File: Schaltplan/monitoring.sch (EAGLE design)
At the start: 10 parts, among them IC1 TINY26P, IC2 7805TV

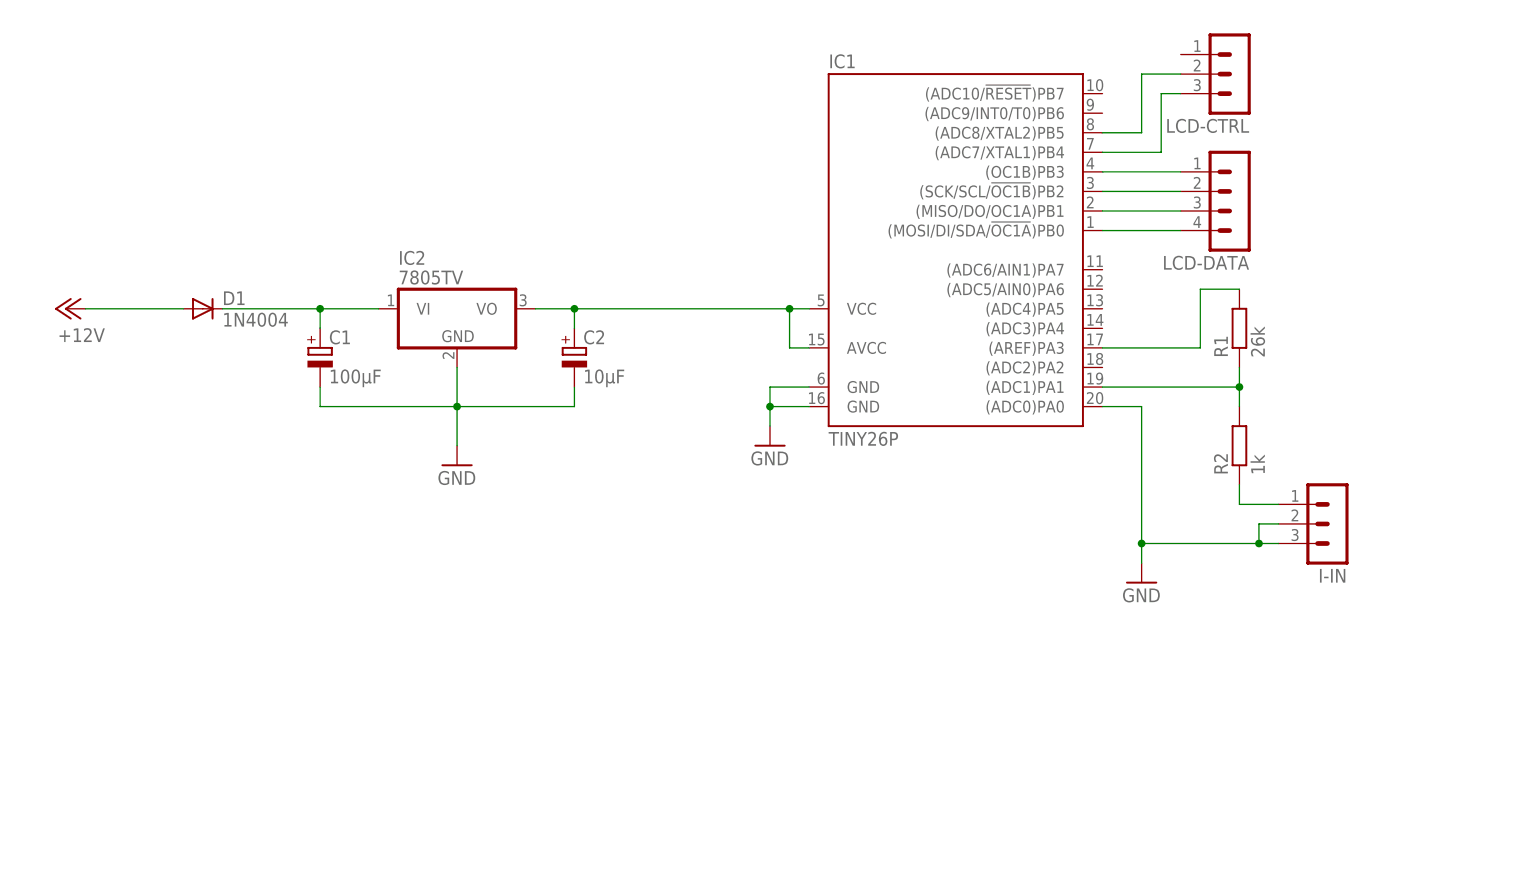
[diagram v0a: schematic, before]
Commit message: Add some induktivits to filter the adc inputs
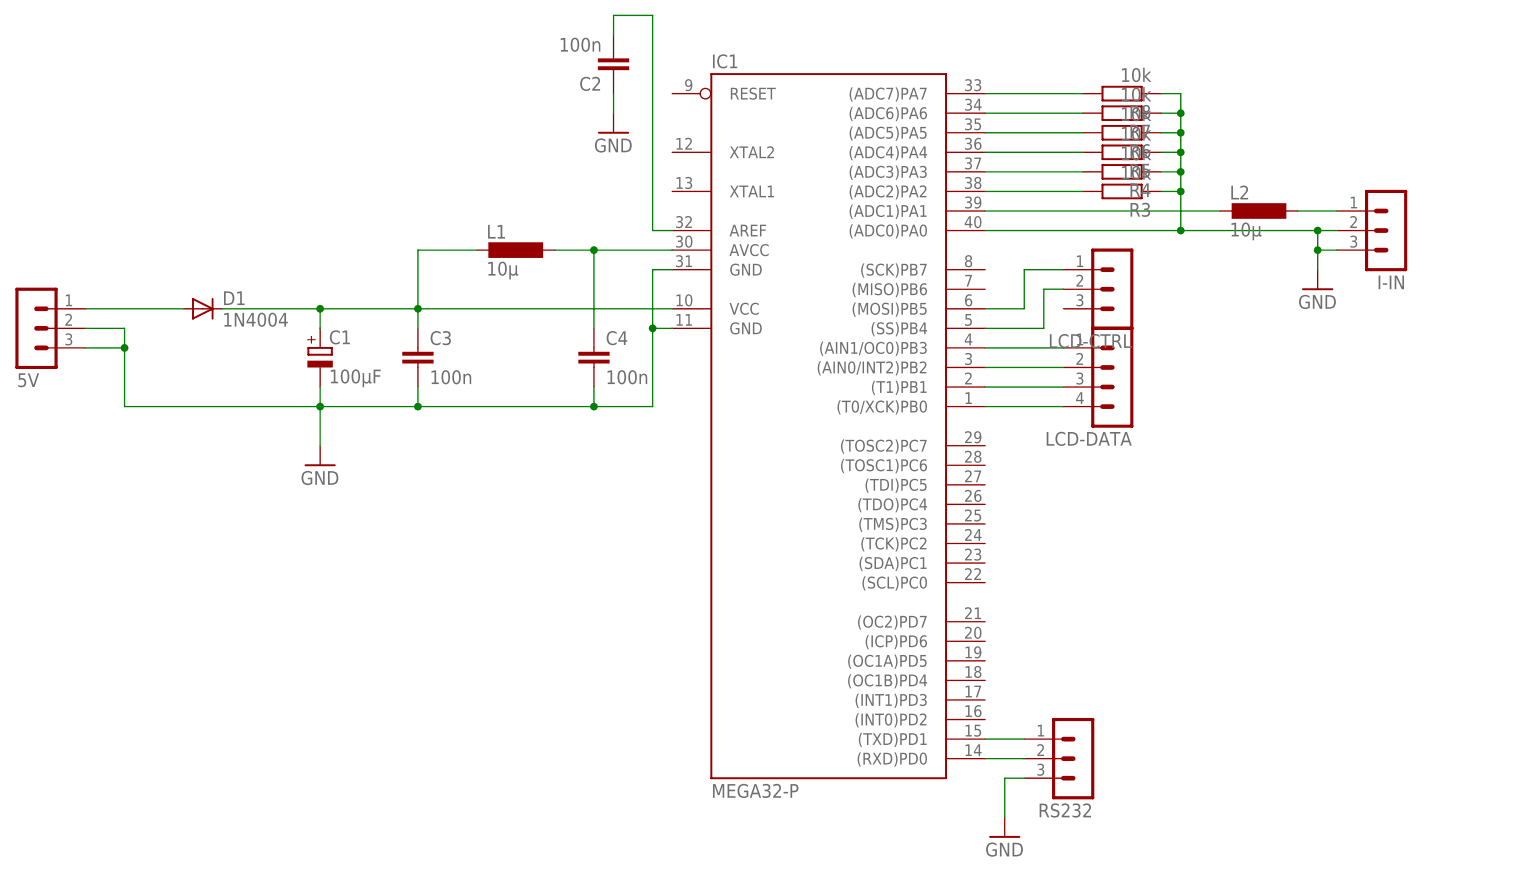
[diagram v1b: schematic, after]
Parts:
- removed IC2: 7805TV, linear:7805TV
- removed R1: 26k, rcl:R-EU_0204/2V
- removed R2: 1k, rcl:R-EU_0204/2V
- added 5V, RS232: (no value), con-lstb:MA03-1
- added C3, C4: 100n, rcl:C-EU050-035X075
- added L1, L2: 10µ, rcl:L-EU0204V
- added R3, R4, R5, R6, R7, R8: 10k, rcl:R-EU_0204/2V
- C2: value 10µF -> 100n; device rcl:CPOL-EUE2.5-7 -> rcl:C-EU050-035X075
- IC1: value TINY26P -> MEGA32-P; device atmel:TINY26P -> atmel:MEGA32-P
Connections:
- removed net +12V: D1.A
- new net N$12: 5V.1, D1.A
- new net N$13: IC1.(ADC4)PA4, R5.2
- new net N$14: C2.2, IC1.AREF
- new net N$15: IC1.(RXD)PD0, RS232.2
- new net N$16: IC1.(TXD)PD1, RS232.1
- new net N$17: IC1.(ADC5)PA5, R6.2
- new net N$18: IC1.(ADC6)PA6, R7.2
- new net N$19: IC1.(ADC7)PA7, R8.2
- new net N$20: C4.1, IC1.AVCC, L1.1
- net GND: now also 5V.2, 5V.3, C2.1, C3.2, C4.2, R3.1, R4.1, R5.1, R6.1, R7.1, R8.1, RS232.3; no longer C2.-, IC2.GND
- net N$1: now also IC1.(AIN1/OC0)PB3, LCD-DATA.1; no longer IC1.(MOSI/DI/SDA/!OC1A!)PB0, LCD-DATA.4
- net N$10: now also IC1.(SS)PB4, LCD-CTRL.2; no longer IC1.(ADC7/XTAL1)PB4, LCD-CTRL.3
- net N$11: now also IC1.(MOSI)PB5, LCD-CTRL.1; no longer IC1.(ADC8/XTAL2)PB5, LCD-CTRL.2
- net N$2: now also C1.+, C3.1, D1.C, L1.2; no longer C2.+, IC1.AVCC, IC2.VO
- net N$3: now also IC1.(ADC2)PA2, R3.2; no longer C1.+, D1.C, IC2.VI
- net N$4: now also IC1.(AIN0/INT2)PB2, LCD-DATA.2; no longer IC1.(MISO/DO/OC1A)PB1, LCD-DATA.3
- net N$5: now also L2.2; no longer R1.1, R2.2
- net N$6: now also IC1.(ADC3)PA3, R4.2; no longer IC1.(AREF)PA3, R1.2
- net N$7: now also L2.1; no longer R2.1
- net N$8: now also IC1.(T1)PB1, LCD-DATA.3; no longer IC1.(SCK/SCL/!OC1B!)PB2, LCD-DATA.2
- net N$9: now also IC1.(T0/XCK)PB0, LCD-DATA.4; no longer IC1.(OC1B)PB3, LCD-DATA.1
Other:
- moved on the sheet: I-IN, LCD-CTRL, LCD-DATA

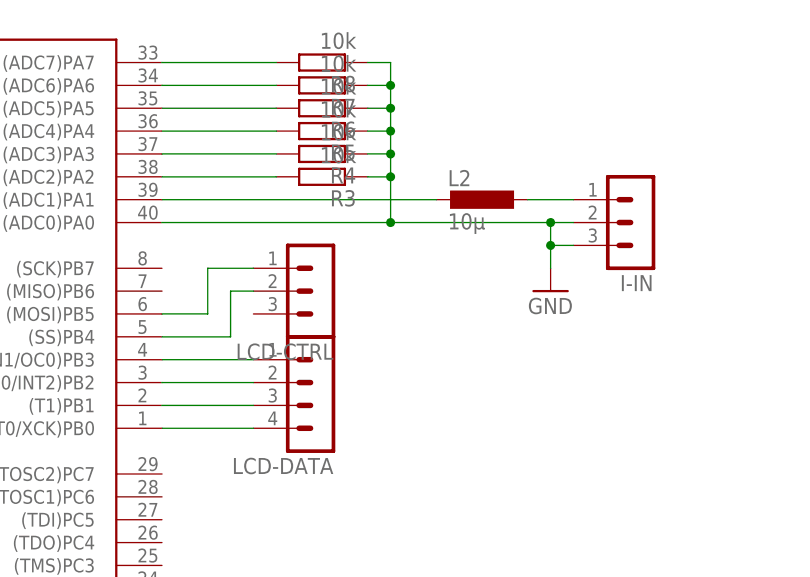
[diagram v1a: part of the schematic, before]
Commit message: Use a median filter and an irr filter for the adc value which measures the current
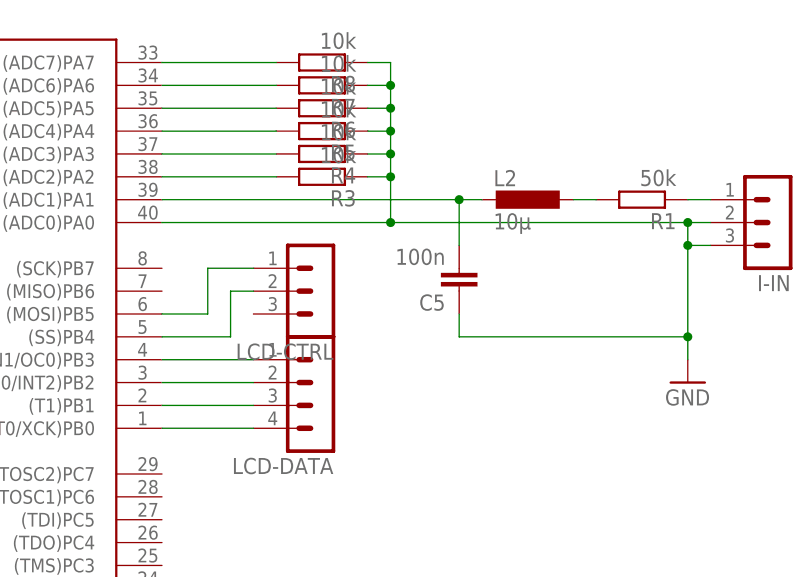
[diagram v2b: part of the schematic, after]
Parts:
- added C5: 100n, rcl:C-EU050-035X075
- added R1: 50k, rcl:R-EU_0204/2V
- L2: device rcl:L-EU0204V -> rcl:L-EU0207/10
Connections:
- removed net N$7: I-IN.1, L2.1
- new net N$21: L2.1, R1.2
- new net N$22: I-IN.1, R1.1
- net GND: now also C5.1
- net N$5: now also C5.2
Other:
- moved on the sheet: I-IN, L2
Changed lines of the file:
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@@
 <grid distance="0.1" unitdist="inch" unit="inch" style="lines" multiple="1" display="no" altdistance="0.01" altunitdist="inch" altunit="inch"/>
 <layers>
-<layer number="1" name="Top" color="4" fill="1" visible="no" active="no"/>
-<layer number="16" name="Bottom" color="1" fill="1" visible="no" active="no"/>
-<layer number="17" name="Pads" color="2" fill="1" visible="no" active="no"/>
-<layer number="18" name="Vias" color="2" fill="1" visible="no" active="no"/>
-<layer number="19" name="Unrouted" color="6" fill="1" visible="no" active="no"/>
-<layer number="20" name="Dimension" color="15" fill="1" visible="no" active="no"/>
-<layer number="21" name="tPlace" color="7" fill="1" visible="no" active="no"/>
-<layer number="22" name="bPlace" color="7" fill="1" visible="no" active="no"/>
-<layer number="23" name="tOrigins" color="15" fill="1" visible="no" active="no"/>
-<layer number="24" name="bOrigins" color="15" fill="1" visible="no" active="no"/>
-<layer number="25" name="tNames" color="7" fill="1" visible="no" active="no"/>
-<layer number="26" name="bNames" color="7" fill="1" visible="no" active="no"/>
-<layer number="27" name="tValues" color="7" fill="1" visible="no" active="no"/>
-<layer number="28" name="bValues" color="7" fill="1" visible="no" active="no"/>
+<layer number="1" name="Top" color="4" fill="1" visible="yes" active="no"/>
+<layer number="16" name="Bottom" color="1" fill="1" visible="yes" active="no"/>
+<layer number="17" name="Pads" color="2" fill="1" visible="yes" active="no"/>
+<layer number="18" name="Vias" color="2" fill="1" visible="yes" active="no"/>
+<layer number="19" name="Unrouted" color="6" fill="1" visible="yes" active="no"/>
+<layer number="20" name="Dimension" color="15" fill="1" visible="yes" active="no"/>
+<layer number="21" name="tPlace" color="7" fill="1" visible="yes" active="no"/>
+<layer number="22" name="bPlace" color="7" fill="1" visible="yes" active="no"/>
+<layer number="23" name="tOrigins" color="15" fill="1" visible="yes" active="no"/>
+<layer number="24" name="bOrigins" color="15" fill="1" visible="yes" active="no"/>
+<layer number="25" name="tNames" color="7" fill="1" visible="yes" active="no"/>
+<layer number="26" name="bNames" color="7" fill="1" visible="yes" active="no"/>
+<layer number="27" name="tValues" color="7" fill="1" visible="yes" active="no"/>
+<layer number="28" name="bValues" color="7" fill="1" visible="yes" active="no"/>
 <layer number="29" name="tStop" color="7" fill="3" visible="no" active="no"/>
 <layer number="30" name="bStop" color="7" fill="6" visible="no" active="no"/>
@@
 <layer number="35" name="tGlue" color="7" fill="4" visible="no" active="no"/>
 <layer number="36" name="bGlue" color="7" fill="5" visible="no" active="no"/>
-<layer number="37" name="tTest" color="7" fill="1" visible="no" active="no"/>
-<layer number="38" name="bTest" color="7" fill="1" visible="no" active="no"/>
+<layer number="37" name="tTest" color="7" fill="1" visible="yes" active="no"/>
+<layer number="38" name="bTest" color="7" fill="1" visible="yes" active="no"/>
 <layer number="39" name="tKeepout" color="4" fill="11" visible="no" active="no"/>
 <layer number="40" name="bKeepout" color="1" fill="11" visible="no" active="no"/>
@@
 <layer number="44" name="Drills" color="7" fill="1" visible="no" active="no"/>
 <layer number="45" name="Holes" color="7" fill="1" visible="no" active="no"/>
-<layer number="46" name="Milling" color="3" fill="1" visible="no" active="no"/>
-<layer number="47" name="Measures" color="7" fill="1" visible="no" active="no"/>
-<layer number="48" name="Document" color="7" fill="1" visible="no" active="no"/>
-<layer number="49" name="Reference" color="7" fill="1" visible="no" active="no"/>
-<layer number="51" name="tDocu" color="7" fill="1" visible="no" active="no"/>
-<layer number="52" name="bDocu" color="7" fill="1" visible="no" active="no"/>
+<layer number="46" name="Milling" color="3" fill="1" visible="yes" active="no"/>
+<layer number="47" name="Measures" color="7" fill="1" visible="yes" active="no"/>
+<layer number="48" name="Document" color="7" fill="1" visible="yes" active="no"/>
+<layer number="49" name="Reference" color="7" fill="1" visible="yes" active="no"/>
+<layer number="51" name="tDocu" color="7" fill="1" visible="yes" active="no"/>
+<layer number="52" name="bDocu" color="7" fill="1" visible="yes" active="no"/>
 <layer number="91" name="Nets" color="2" fill="1" visible="yes" active="yes"/>
 <layer number="92" name="Busses" color="1" fill="1" visible="yes" active="yes"/>
@@
 <part name="C4" library="rcl" deviceset="C-EU" device="050-035X075" value="100n"/>
 <part name="L1" library="rcl" deviceset="L-EU" device="0204V" value="10µ"/>
-<part name="L2" library="rcl" deviceset="L-EU" device="0204V" value="10µ"/>
+<part name="L2" library="rcl" deviceset="L-EU" device="0207/10" value="10µ"/>
+<part name="R1" library="rcl" deviceset="R-EU_" device="0204/2V" value="50k"/>
+<part name="C5" library="rcl" deviceset="C-EU" device="050-035X075" value="100n"/>
 </parts>
 <sheets>
@@
 <instance part="GND1" gate="1" x="-17.78" y="25.4"/>
 <instance part="C1" gate="G$1" x="-17.78" y="40.64"/>
-<instance part="GND3" gate="1" x="111.76" y="48.26"/>
-<instance part="I-IN" gate="G$1" x="121.92" y="55.88" rot="R180"/>
+<instance part="GND3" gate="1" x="127" y="38.1"/>
+<instance part="I-IN" gate="G$1" x="137.16" y="55.88" rot="R180"/>
 <instance part="LCD-DATA" gate="1" x="86.36" y="35.56" rot="R180"/>
 <instance part="LCD-CTRL" gate="G$1" x="86.36" y="48.26" rot="R180"/>
@@
 <instance part="C4" gate="G$1" x="17.78" y="40.64"/>
 <instance part="L1" gate="G$1" x="7.62" y="53.34" rot="R270"/>
-<instance part="L2" gate="G$1" x="104.14" y="58.42" rot="R270"/>
+<instance part="L2" gate="G$1" x="109.22" y="58.42" rot="R270"/>
+<instance part="R1" gate="G$1" x="121.92" y="58.42" rot="R180"/>
+<instance part="C5" gate="G$1" x="101.6" y="48.26" rot="R180"/>
 </instances>
 <busses>
@@
 <pinref part="I-IN" gate="G$1" pin="2"/>
 <pinref part="GND3" gate="1" pin="GND"/>
-<wire x1="93.98" y1="55.88" x2="111.76" y2="55.88" width="0.1524" layer="91"/>
-<wire x1="111.76" y1="55.88" x2="114.3" y2="55.88" width="0.1524" layer="91"/>
-<wire x1="111.76" y1="50.8" x2="111.76" y2="53.34" width="0.1524" layer="91"/>
-<junction x="111.76" y="55.88"/>
+<wire x1="93.98" y1="55.88" x2="127" y2="55.88" width="0.1524" layer="91"/>
+<wire x1="127" y1="55.88" x2="129.54" y2="55.88" width="0.1524" layer="91"/>
+<wire x1="127" y1="40.64" x2="127" y2="43.18" width="0.1524" layer="91"/>
+<junction x="127" y="55.88"/>
 <pinref part="I-IN" gate="G$1" pin="3"/>
-<wire x1="111.76" y1="53.34" x2="111.76" y2="55.88" width="0.1524" layer="91"/>
-<wire x1="114.3" y1="53.34" x2="111.76" y2="53.34" width="0.1524" layer="91"/>
-<junction x="111.76" y="53.34"/>
+<wire x1="127" y1="43.18" x2="127" y2="53.34" width="0.1524" layer="91"/>
+<wire x1="127" y1="53.34" x2="127" y2="55.88" width="0.1524" layer="91"/>
+<wire x1="129.54" y1="53.34" x2="127" y2="53.34" width="0.1524" layer="91"/>
+<junction x="127" y="53.34"/>
 <pinref part="R8" gate="G$1" pin="1"/>
 <wire x1="91.44" y1="73.66" x2="93.98" y2="73.66" width="0.1524" layer="91"/>
@@
 <wire x1="68.58" y1="55.88" x2="93.98" y2="55.88" width="0.1524" layer="91"/>
 <junction x="93.98" y="55.88"/>
+<pinref part="C5" gate="G$1" pin="1"/>
+<wire x1="101.6" y1="45.72" x2="101.6" y2="43.18" width="0.1524" layer="91"/>
+<wire x1="101.6" y1="43.18" x2="127" y2="43.18" width="0.1524" layer="91"/>
+<junction x="127" y="43.18"/>
 </segment>
 <segment>
@@
 <net name="N$5" class="0">
 <segment>
-<wire x1="68.58" y1="58.42" x2="99.06" y2="58.42" width="0.1524" layer="91"/>
+<wire x1="68.58" y1="58.42" x2="101.6" y2="58.42" width="0.1524" layer="91"/>
 <pinref part="IC1" gate="G$1" pin="(ADC1)PA1"/>
 <pinref part="L2" gate="G$1" pin="2"/>
-</segment>
-</net>
-<net name="N$7" class="0">
-<segment>
-<pinref part="I-IN" gate="G$1" pin="1"/>
-<wire x1="114.3" y1="58.42" x2="109.22" y2="58.42" width="0.1524" layer="91"/>
-<pinref part="L2" gate="G$1" pin="1"/>
+<pinref part="C5" gate="G$1" pin="2"/>
+<wire x1="101.6" y1="58.42" x2="104.14" y2="58.42" width="0.1524" layer="91"/>
+<wire x1="101.6" y1="53.34" x2="101.6" y2="58.42" width="0.1524" layer="91"/>
+<junction x="101.6" y="58.42"/>
 </segment>
 </net>
@@
 </segment>
 </net>
+<net name="N$21" class="0">
+<segment>
+<pinref part="R1" gate="G$1" pin="2"/>
+<pinref part="L2" gate="G$1" pin="1"/>
+<wire x1="116.84" y1="58.42" x2="114.3" y2="58.42" width="0.1524" layer="91"/>
+</segment>
+</net>
+<net name="N$22" class="0">
+<segment>
+<pinref part="R1" gate="G$1" pin="1"/>
+<pinref part="I-IN" gate="G$1" pin="1"/>
+<wire x1="127" y1="58.42" x2="129.54" y2="58.42" width="0.1524" layer="91"/>
+</segment>
+</net>
